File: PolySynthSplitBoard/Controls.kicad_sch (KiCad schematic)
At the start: 105 parts, among them SW601 ENV1_B, SW602 ENV2_B, SW603 HP_B, SW604 LFO1_B, SW605 LFO2_B, SW606 HP_B, SW607 LFO3_B, SW608 FF_B, SW609 MIX1_B, SW610 MIX2_B, SW611 ENC_MENU, SW612 ALT_B, U601 MCP23S17_SS, U602 MCP23S17_SS, U603 ILI9341

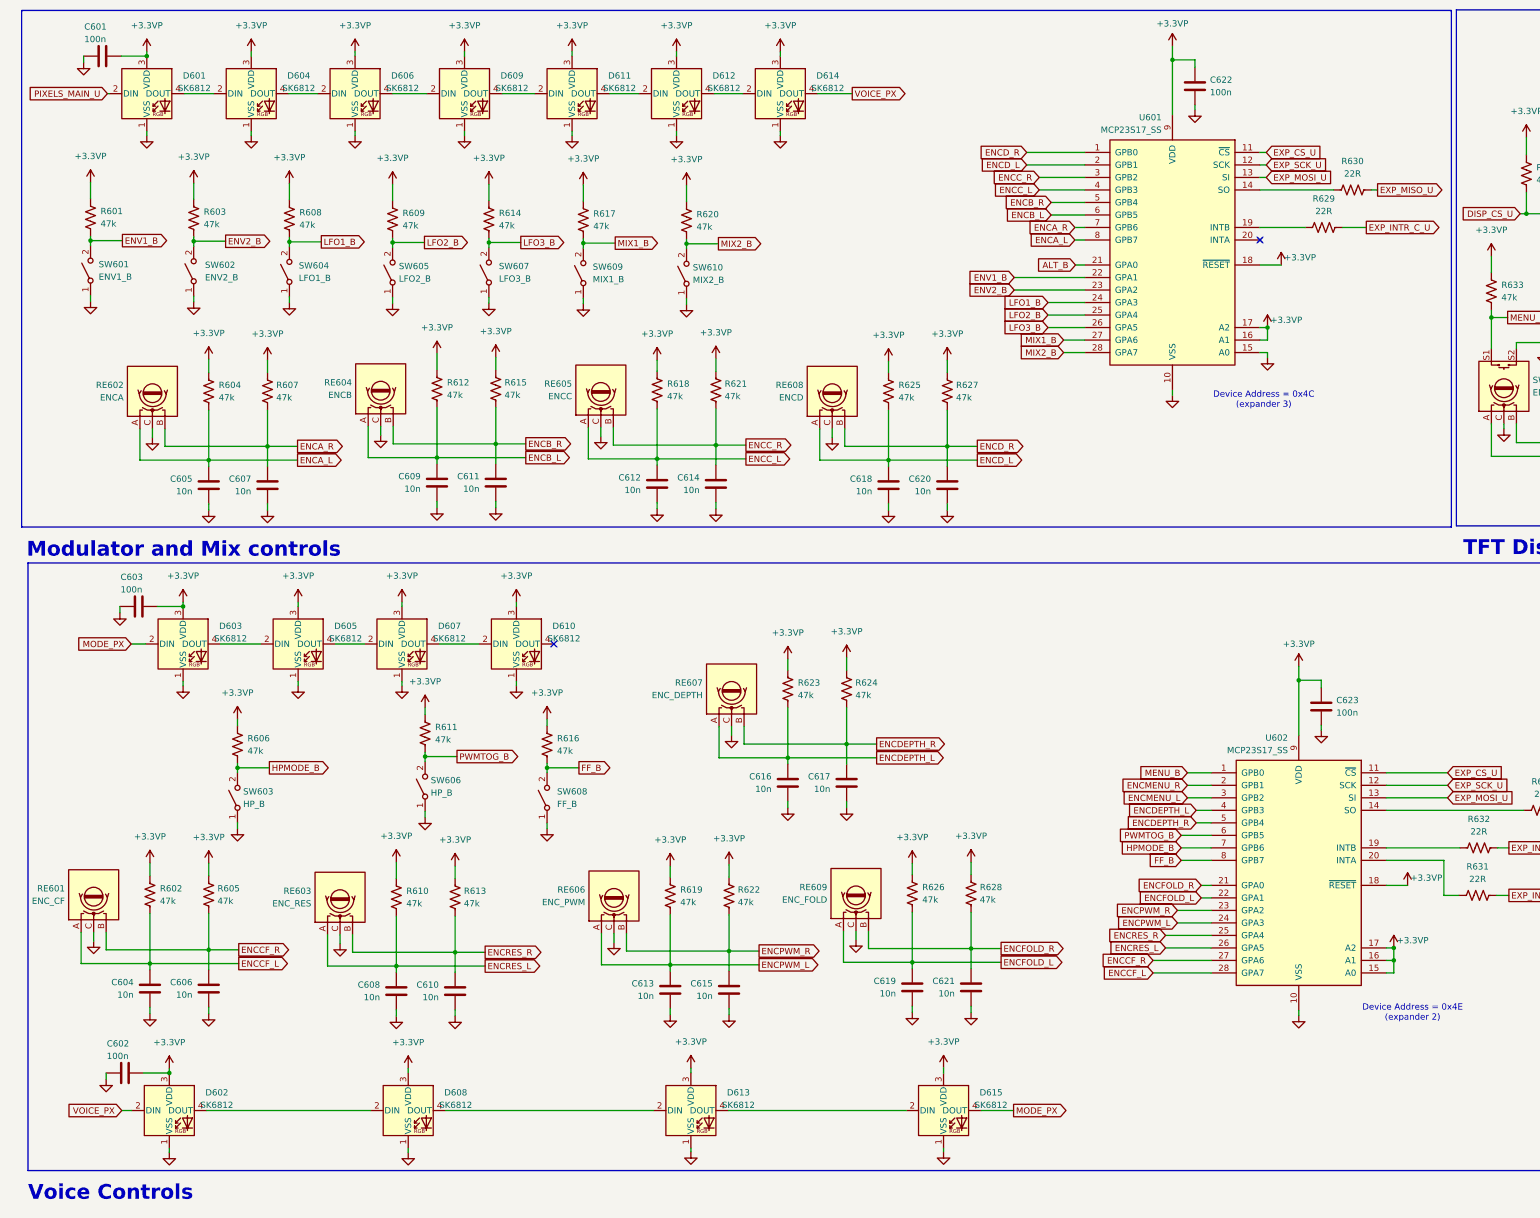
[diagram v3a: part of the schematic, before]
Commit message: switching to 20p mezzanine connectors
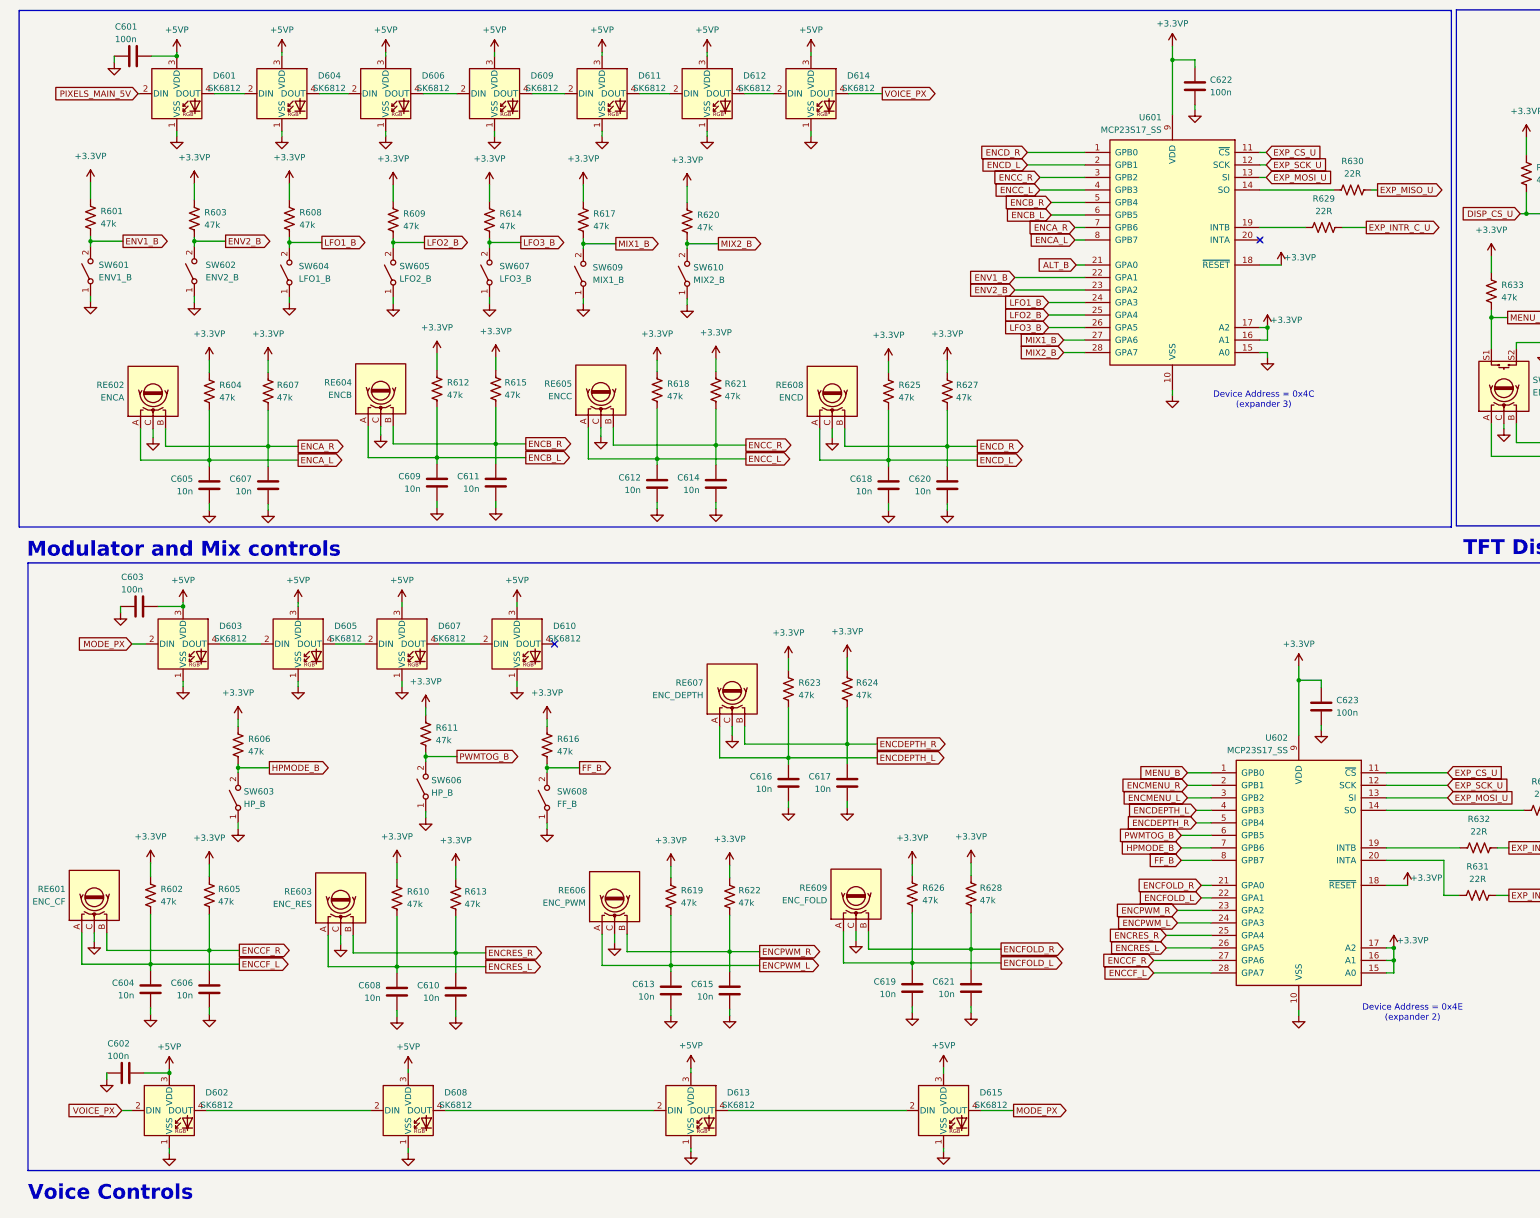
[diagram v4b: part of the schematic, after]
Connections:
- net +3.3VP: no longer C601.2, C602.2, C603.2, D601.3 (VDD), D602.3 (VDD), D603.3 (VDD), D604.3 (VDD), D605.3 (VDD), D606.3 (VDD), D607.3 (VDD), D608.3 (VDD), D609.3 (VDD), D610.3 (VDD), D611.3 (VDD), D612.3 (VDD), D613.3 (VDD), D614.3 (VDD), D615.3 (VDD)
- net PIXELS_MAIN_U renamed PIXELS_MAIN_5V
- new net +5VP: C601.2, C602.2, C603.2, D601.3 (VDD), D602.3 (VDD), D603.3 (VDD), D604.3 (VDD), D605.3 (VDD), D606.3 (VDD), D607.3 (VDD), D608.3 (VDD), D609.3 (VDD), D610.3 (VDD), D611.3 (VDD), D612.3 (VDD), D613.3 (VDD), D614.3 (VDD), D615.3 (VDD)
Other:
- moved on the sheet: C601, D601, D604, D606, D609, D611, D612, D614

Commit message: rev2 motherboard sent to fab
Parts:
- added C628: 100n, Capacitor_SMD:C_0805_2012Metric, symbol Device:C
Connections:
- net +5VP: now also C628.2
- net GNDA: now also C628.1
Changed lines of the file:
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@@
 	)
 	(junction
+		(at 109.22 24.384)
+		(diameter 0)
+		(color 0 0 0 0)
+	)
+	(junction
 		(at 266.192 80.772)
 		(diameter 0)
@@
 	(wire
 		(pts
+			(xy 109.22 24.384) (xy 109.22 25.654)
+		)
+		(stroke
+			(width 0)
+			(type default)
+		)
+	)
+	(wire
+		(pts
 			(xy 251.714 181.356) (xy 254.762 181.356)
 		)
@@
 	(wire
 		(pts
-			(xy 109.22 24.892) (xy 109.22 25.654)
+			(xy 109.22 22.86) (xy 109.22 24.384)
 		)
 		(stroke
@@
 	(wire
 		(pts
+			(xy 100.838 24.384) (xy 100.838 25.654)
+		)
+		(stroke
+			(width 0)
+			(type default)
+		)
+	)
+	(wire
+		(pts
 			(xy 51.308 207.264) (xy 51.308 199.898)
 		)
@@
 	(wire
 		(pts
+			(xy 108.458 24.384) (xy 109.22 24.384)
+		)
+		(stroke
+			(width 0)
+			(type default)
+		)
+	)
+	(wire
+		(pts
 			(xy 73.66 33.274) (xy 79.502 33.274)
 		)
@@
 	)
 	(symbol
+		(lib_id "Device:C")
+		(at 104.648 24.384 90)
+		(unit 1)
+		(exclude_from_sim no)
+		(in_bom yes)
+		(on_board yes)
+		(dnp no)
+		(property "Reference" "C628"
+			(at 100.965 18.415 90)
+			(effects
+				(font
+					(size 1.27 1.27)
+				)
+				(justify right)
+			)
+		)
+		(property "Value" "100n"
+			(at 100.965 20.955 90)
+			(effects
+				(font
+					(size 1.27 1.27)
+				)
+				(justify right)
+			)
+		)
+		(property "Footprint" "Capacitor_SMD:C_0805_2012Metric"
+			(at 108.458 23.4188 0)
+			(effects
+				(font
+					(size 1.27 1.27)
+				)
+				(hide yes)
+			)
+		)
+		(property "Datasheet" "~"
+			(at 104.648 24.384 0)
+			(effects
+				(font
+					(size 1.27 1.27)
+				)
+				(hide yes)
+			)
+		)
+		(property "Description" ""
+			(at 104.648 24.384 0)
+			(effects
+				(font
+					(size 1.27 1.27)
+				)
+				(hide yes)
+			)
+		)
+		(pin "1"
+		)
+		(pin "2"
+		)
+		(instances
+			(project "PolySynthSplitBoard"
+				(path "/22649217-9810-470f-bc7b-6f743ad2b90e/db382c1e-7a8e-4aae-96bd-96ec756a5476/f9611335-018a-4682-8f39-2088bfa85de9"
+					(reference "C628")
+					(unit 1)
+				)
+			)
+		)
+	)
+	(symbol
 		(lib_id "Device:R_US")
 		(at 88.646 58.928 0)
@@
 	)
 	(symbol
+		(lib_id "power:GND")
+		(at 100.838 25.654 0)
+		(unit 1)
+		(exclude_from_sim no)
+		(in_bom yes)
+		(on_board yes)
+		(dnp no)
+		(fields_autoplaced yes)
+		(property "Reference" "#PWR0870"
+			(at 100.838 32.004 0)
+			(effects
+				(font
+					(size 1.27 1.27)
+				)
+				(hide yes)
+			)
+		)
+		(property "Value" "GNDA"
+			(at 100.838 29.464 0)
+			(effects
+				(font
+					(size 1.27 1.27)
+				)
+				(hide yes)
+			)
+		)
+		(property "Footprint" ""
+			(at 100.838 25.654 0)
+			(effects
+				(font
+					(size 1.27 1.27)
+				)
+				(hide yes)
+			)
+		)
+		(property "Datasheet" ""
+			(at 100.838 25.654 0)
+			(effects
+				(font
+					(size 1.27 1.27)
+				)
+				(hide yes)
+			)
+		)
+		(property "Description" ""
+			(at 100.838 25.654 0)
+			(effects
+				(font
+					(size 1.27 1.27)
+				)
+				(hide yes)
+			)
+		)
+		(pin "1"
+		)
+		(instances
+			(project "PolySynthSplitBoard"
+				(path "/22649217-9810-470f-bc7b-6f743ad2b90e/db382c1e-7a8e-4aae-96bd-96ec756a5476/f9611335-018a-4682-8f39-2088bfa85de9"
+					(reference "#PWR0870")
+					(unit 1)
+				)
+			)
+		)
+	)
+	(symbol
 		(lib_id "Device:C")
 		(at 109.474 112.268 0)
@@
 	(symbol
 		(lib_id "power:+5VP")
-		(at 109.22 24.892 0)
+		(at 109.22 22.86 0)
 		(unit 1)
 		(exclude_from_sim no)
@@
 		(fields_autoplaced yes)
 		(property "Reference" "#PWR0697"
-			(at 109.22 28.702 0)
+			(at 109.22 26.67 0)
 			(effects
 				(font
@@
 		)
 		(property "Value" "+5VP"
-			(at 109.22 20.32 0)
+			(at 109.22 18.288 0)
 			(effects
 				(font
@@
 		)
 		(property "Footprint" ""
-			(at 109.22 24.892 0)
+			(at 109.22 22.86 0)
 			(effects
 				(font
@@
 		)
 		(property "Datasheet" ""
-			(at 109.22 24.892 0)
+			(at 109.22 22.86 0)
 			(effects
 				(font
@@
 		)
 		(property "Description" "Power symbol creates a global label with name \"+5VP\""
-			(at 109.22 24.892 0)
+			(at 109.22 22.86 0)
 			(effects
 				(font
